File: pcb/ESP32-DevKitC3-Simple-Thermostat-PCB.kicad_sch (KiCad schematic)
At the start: 52 parts, among them J1 PINHD_1x18_Male, J2 Screw_Terminal_9_P3.50mm, J3 DS18B20, J4 3.2 lcd tft, J5 AHT20 Board, J6 LD2410C, K1 G5Q-1A, K2 G5Q-1A, K3 G5Q-1A, K4 G5Q-1A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

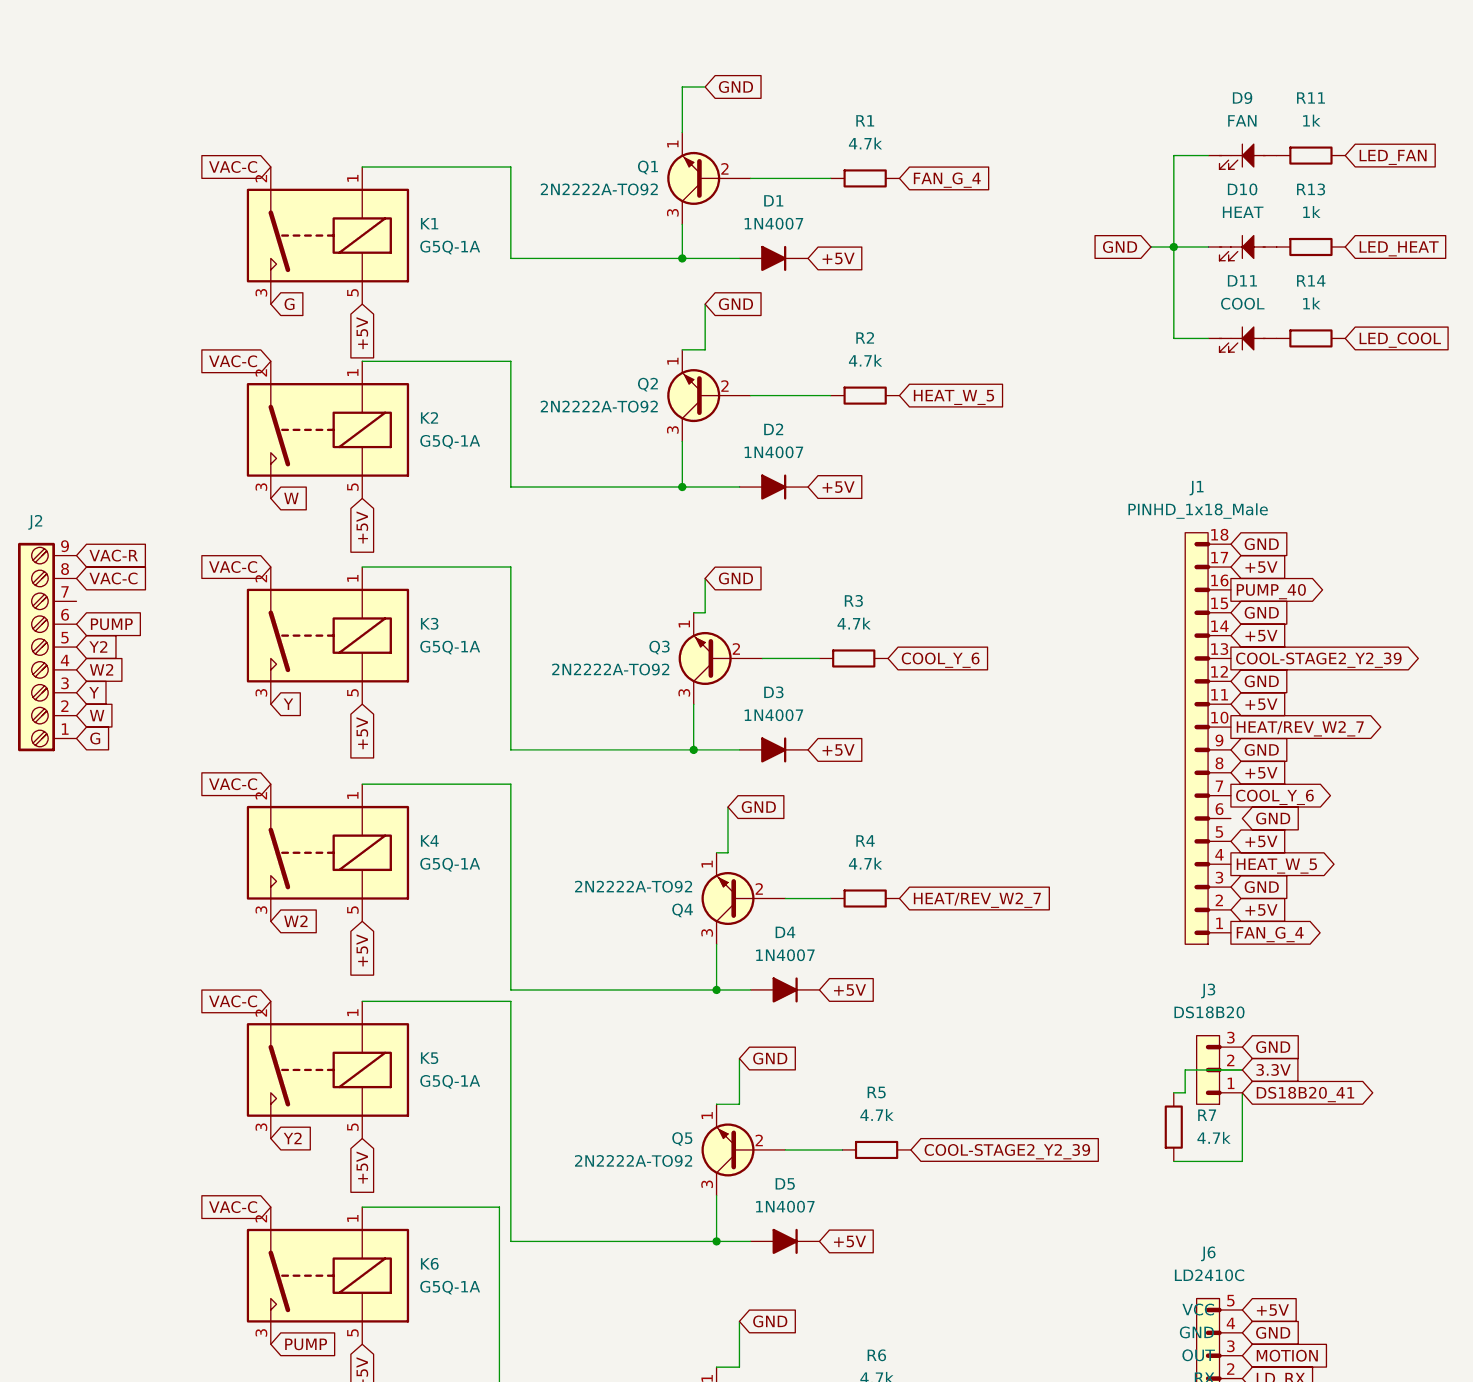
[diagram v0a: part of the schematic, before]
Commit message: add relay common and split c input
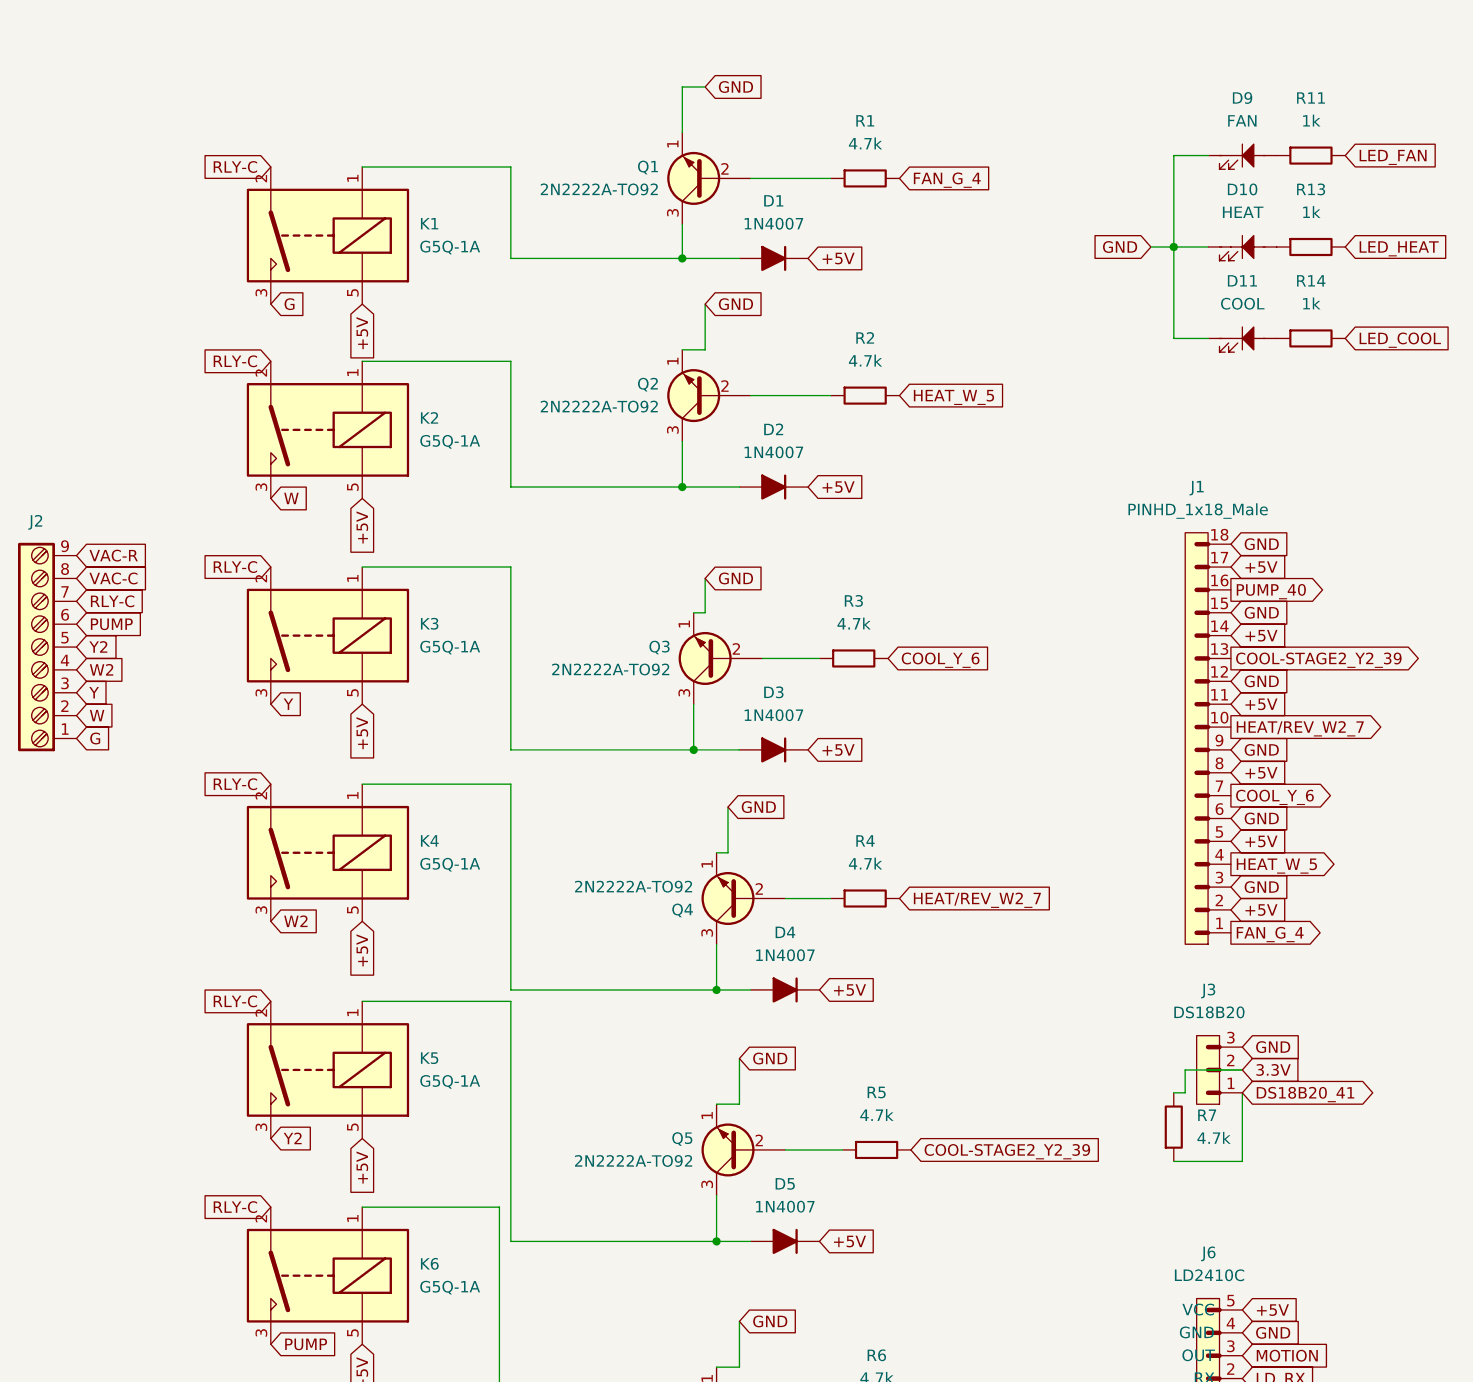
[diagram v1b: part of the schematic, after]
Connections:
- net GND: now also J1.6
- net VAC-C: no longer K1.2, K2.2, K3.2, K4.2, K5.2, K6.2
- net RLY-C: now reaches J2.7
- net RLY-C: now also K1.2, K2.2, K3.2, K4.2, K5.2, K6.2
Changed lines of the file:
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@@
 		)
 	)
-	(global_label "VAC-C"
+	(global_label "RLY-C"
 		(shape input)
 		(at 53.34 52.07 180)
@@
 		)
 		(property "Intersheetrefs" "${INTERSHEET_REFS}"
-			(at 44.0652 52.07 0)
+			(at 44.1257 52.07 0)
 			(effects
 				(font
@@
 		)
 	)
-	(global_label "VAC-C"
+	(global_label "RLY-C"
 		(shape input)
 		(at 53.34 123.19 180)
@@
 		)
 		(property "Intersheetrefs" "${INTERSHEET_REFS}"
-			(at 44.0652 123.19 0)
+			(at 44.1257 123.19 0)
 			(effects
 				(font
@@
 		)
 	)
-	(global_label "VAC-C"
+	(global_label "RLY-C"
 		(shape input)
 		(at 53.34 30.48 180)
@@
 		)
 		(property "Intersheetrefs" "${INTERSHEET_REFS}"
-			(at 44.0652 30.48 0)
+			(at 44.1257 30.48 0)
 			(effects
 				(font
@@
 		)
 	)
-	(global_label "VAC-C"
+	(global_label "RLY-C"
 		(shape input)
 		(at 53.34 74.93 180)
@@
 		)
 		(property "Intersheetrefs" "${INTERSHEET_REFS}"
-			(at 44.0652 74.93 0)
+			(at 44.1257 74.93 0)
 			(effects
 				(font
@@
 		)
 	)
-	(global_label "VAC-C"
+	(global_label "RLY-C"
 		(shape input)
 		(at 53.34 146.05 180)
@@
 		)
 		(property "Intersheetrefs" "${INTERSHEET_REFS}"
-			(at 44.0652 146.05 0)
+			(at 44.1257 146.05 0)
 			(effects
 				(font
@@
 		)
 	)
-	(global_label "VAC-C"
+	(global_label "RLY-C"
 		(shape input)
 		(at 53.34 99.06 180)
@@
 		)
 		(property "Intersheetrefs" "${INTERSHEET_REFS}"
-			(at 44.0652 99.06 0)
+			(at 44.1257 99.06 0)
 			(effects
 				(font
@@
 		)
 	)
+	(global_label "RLY-C"
+		(shape input)
+		(at 31.75 78.74 0)
+		(fields_autoplaced yes)
+		(effects
+			(font
+				(size 1.27 1.27)
+			)
+			(justify left)
+		)
+		(property "Intersheetrefs" "${INTERSHEET_REFS}"
+			(at 40.9643 78.74 0)
+			(effects
+				(font
+					(size 1.27 1.27)
+				)
+				(justify left)
+				(hide yes)
+			)
+		)
+		(property "Netclass" "Contacts"
+			(at 31.75 80.9308 0)
+			(effects
+				(font
+					(size 1.27 1.27)
+				)
+				(justify left)
+				(hide yes)
+			)
+		)
+	)
 	(global_label "LD_TX"
 		(shape input)
@@
 	(global_label "GND"
 		(shape input)
-		(at 161.29 102.87 0)
-		(fields_autoplaced yes)
-		(effects
-			(font
-				(size 1.27 1.27)
-			)
-			(justify left)
-		)
-		(property "Intersheetrefs" "${INTERSHEET_REFS}"
-			(at 168.1457 102.87 0)
-			(effects
-				(font
+		(at 160.02 102.87 0)
+		(fields_autoplaced yes)
+		(effects
+			(font
+				(size 1.27 1.27)
+			)
+			(justify left)
+		)
+		(property "Intersheetrefs" "${INTERSHEET_REFS}"
+			(at 166.8757 102.87 0)
+			(effects
+				(font

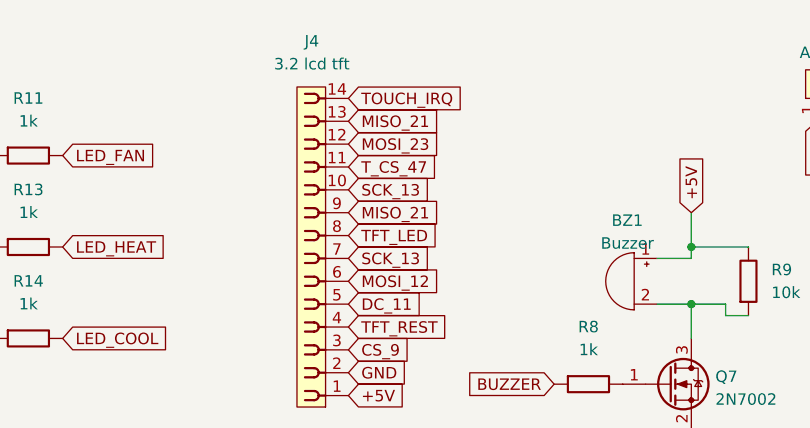
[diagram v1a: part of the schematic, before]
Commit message: Bump version to 1.3.7 - Fix fan relay oscillation bug when manual 'on' mode conflicts with HVAC fan control. Update schermatic and PCB for missing trace.
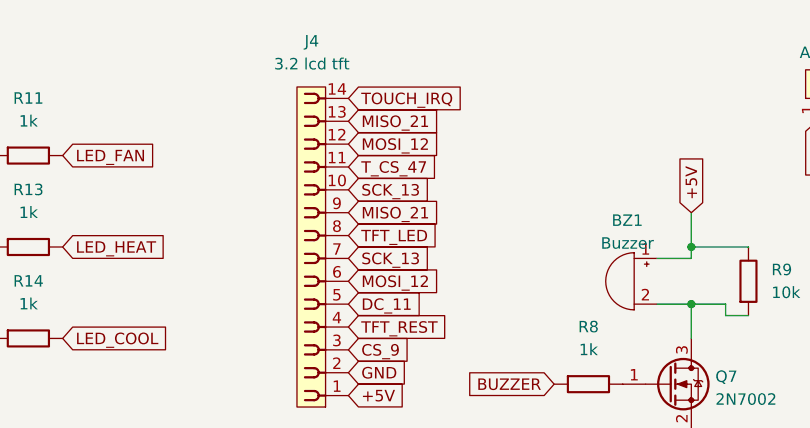
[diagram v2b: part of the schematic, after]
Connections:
- net MOSI_23 is gone; now on net MOSI_12: J4.12
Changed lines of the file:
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@@
 		)
 	)
-	(global_label "MOSI_23"
+	(global_label "MOSI_12"
 		(shape input)
 		(at 204.47 27.94 0)

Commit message: Cleanup old files.
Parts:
- added J7: PINHD_1x3_Male, Connector_PinHeader_2.54mm:PinHeader_1x03_P2.54mm_Vertical, symbol PCM_SL_Pin_Headers:PINHD_1x3_Male
- J5: value AHT20 Board -> I2C Sensor
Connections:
- net +5V: now also J7.1; no longer J5.1
- net 3.3V: now also J7.3
- new net: J5.1, J7.2
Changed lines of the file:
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@@
 	(wire
 		(pts
+			(xy 259.08 36.83) (xy 251.46 36.83)
+		)
+		(stroke
+			(width 0)
+			(type default)
+		)
+	)
+	(wire
+		(pts
+			(xy 251.46 34.29) (xy 256.54 34.29)
+		)
+		(stroke
+			(width 0)
+			(type default)
+		)
+	)
+	(wire
+		(pts
 			(xy 99.06 66.04) (xy 99.06 60.96)
 		)
@@
 	(wire
 		(pts
+			(xy 256.54 34.29) (xy 256.54 25.4)
+		)
+		(stroke
+			(width 0)
+			(type default)
+		)
+	)
+	(wire
+		(pts
 			(xy 228.6 234.95) (xy 189.23 234.95)
 		)
@@
 	(wire
 		(pts
+			(xy 252.73 31.75) (xy 252.73 26.67)
+		)
+		(stroke
+			(width 0)
+			(type default)
+		)
+	)
+	(wire
+		(pts
 			(xy 153.67 133.35) (xy 154.94 133.35)
 		)
@@
 	(wire
 		(pts
+			(xy 252.73 31.75) (xy 251.46 31.75)
+		)
+		(stroke
+			(width 0)
+			(type default)
+		)
+	)
+	(wire
+		(pts
 			(xy 101.6 21.59) (xy 99.06 21.59)
 		)
@@
 	(wire
 		(pts
+			(xy 259.08 38.1) (xy 259.08 36.83)
+		)
+		(stroke
+			(width 0)
+			(type default)
+		)
+	)
+	(wire
+		(pts
 			(xy 106.68 121.92) (xy 102.87 121.92)
 		)
@@
 	(global_label "+5V"
 		(shape input)
-		(at 256.54 25.4 270)
+		(at 259.08 38.1 270)
 		(fields_autoplaced yes)
 		(effects
@@
 		)
 		(property "Intersheetrefs" "${INTERSHEET_REFS}"
-			(at 256.54 32.2557 90)
+			(at 259.08 44.9557 90)
 			(effects
 				(font
@@
 		)
 	)
+	(global_label "3.3V"
+		(shape output)
+		(at 252.73 26.67 90)
+		(fields_autoplaced yes)
+		(effects
+			(font
+				(size 1.27 1.27)
+			)
+			(justify left)
+		)
+		(property "Intersheetrefs" "${INTERSHEET_REFS}"
+			(at 252.73 19.5724 90)
+			(effects
+				(font
+					(size 1.27 1.27)
+				)
+				(justify left)
+				(hide yes)
+			)
+		)
+	)
 	(global_label "GND"
 		(shape input)
@@
 			)
 		)
-		(property "Value" "AHT20 Board"
+		(property "Value" "I2C Sensor"
 			(at 260.35 17.78 90)
 			(effects
@@
 					(unit 1)
 				)
+			)
+		)
+	)
+	(symbol
+		(lib_id "PCM_SL_Pin_Headers:PINHD_1x3_Male")
+		(at 247.65 34.29 180)
+		(unit 1)
+		(exclude_from_sim no)
+		(in_bom yes)
+		(on_board yes)
+		(dnp no)
+		(fields_autoplaced yes)
+		(property "Reference" "J7"
+			(at 247.775 27.94 0)
+			(effects
+				(font
+					(size 1.27 1.27)
+				)
+			)
+		)
+		(property "Value" "PINHD_1x3_Male"
+			(at 247.775 27.94 0)
+			(effects
+				(font
+					(size 1.27 1.27)
+				)
+				(hide yes)
+			)
+		)
+		(property "Footprint" "Connector_PinHeader_2.54mm:PinHeader_1x03_P2.54mm_Vertical"
+			(at 246.38 29.21 0)
+			(effects
+				(font
+					(size 1.27 1.27)
+				)
+				(hide yes)
+			)
+		)
+		(property "Datasheet" ""
+			(at 247.65 43.18 0)
+			(effects
+				(font
+					(size 1.27 1.27)
+				)
+				(hide yes)
+			)
+		)
+		(property "Description" "Pin Header male with pin space 2.54mm. Pin Count -3"
+			(at 247.65 34.29 0)
+			(effects
+				(font
+					(size 1.27 1.27)
+				)
+				(hide yes)
+			)
+		)
+		(pin "1"
+		)
+		(pin "2"
+		)
+		(pin "3"
+		)
+		(instances
+			(project ""
+				(path "/03f971b2-48ed-4915-b0f1-49bc6f8499e8"
+					(reference "J7")
+					(unit 1)
+				)

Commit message: Update PCB and remove extra 3.3v netlist.
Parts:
- R12: value LDR07 -> GL5537
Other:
- moved on the sheet: BZ1, C5, C6, C8, C9, D1, D10, D11, D2, D3, D4, D5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
